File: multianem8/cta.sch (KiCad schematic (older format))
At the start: 281 parts, among them Q1 TIP41, Q10 TIP41, Q11 TIP41, Q12 TIP41, Q13 TIP41, Q14 TIP41, Q15 TIP41, Q16 TIP41, Q2 TIP41, Q3 TIP41, Q4 TIP41, Q5 TIP41, Q6 TIP41, Q7 TIP41, Q8 TIP41, Q9 TIP41, U1 LM324, U10 LM324, U11 LM324, U12 LM324, U13 LM324, U14 LM324, U15 LM324, U16 LM324, U2 LM324, U3 LM324, U4 LM324, U5 LM324, U6 LM324, U7 LM324, U8 LM324, U9 LM324

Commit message: Created the multiname8 board
I recycled the multinam16 board and the numbering of each anemometer's component is 1-4 and 9-12. I might (might...) change the numbering 9-12 to 5-8. The output is also inverted inthe flat cable coming out of the board.
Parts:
- removed CI13, CI14, CI15, CI16, CI5, CI6, CI7, CI8: 100n, Capacitor_THT:C_Rect_L7.2mm_W3.5mm_P5.00mm_FKS2_FKP2_MKS2_MKP2, symbol Device:C
- removed Cf13, Cf14, Cf15, Cf16, Cf5, Cf6, Cf7, Cf8: 1u, Capacitor_THT:CP_Radial_D5.0mm_P2.50mm, symbol Device:CP
- removed Cua13, Cua14, Cua15, Cua16, Cua5, Cua6, Cua7, Cua8, Cub13, Cub14, Cub15, Cub16, Cub5, Cub6, Cub7, Cub8: 100n, Capacitor_THT:C_Disc_D5.0mm_W2.5mm_P2.50mm, symbol Device:C
- removed Don13, Don14, Don15, Don16, Don5, Don6, Don7, Don8: 1N4148, Diode_THT:D_DO-35_SOD27_P7.62mm_Horizontal, symbol Diode:1N4148
- removed JOUT1, JOUT2: Conn_01x08, Connector_PinHeader_2.54mm:PinHeader_1x08_P2.54mm_Vertical, symbol Connector_Generic:Conn_01x08
- removed Jw13, Jw14, Jw15, Jw16, Jw5, Jw6, Jw7, Jw8: Conn_01x02, Connector_PinHeader_2.54mm:PinHeader_1x02_P2.54mm_Vertical, symbol Connector_Generic:Conn_01x02
- removed Q13, Q14, Q15, Q16, Q5, Q6, Q7, Q8: TIP41, Package_TO_SOT_THT:TO-220-3_Vertical, symbol Transistor_BJT:TIP41
- removed Ra13, Ra14, Ra15, Ra16, Ra5, Ra6, Ra7, Ra8: 100, Resistor_THT:R_Axial_DIN0207_L6.3mm_D2.5mm_P10.16mm_Horizontal, symbol Device:R
- removed Rb13, Rb14, Rb15, Rb16, Rb5, Rb6, Rb7, Rb8: 10, Resistor_THT:R_Axial_DIN0414_L11.9mm_D4.5mm_P15.24mm_Horizontal, symbol Device:R
- removed Rc13, Rc14, Rc15, Rc16, Rc5, Rc6, Rc7, Rc8: 1k, Resistor_THT:R_Axial_DIN0207_L6.3mm_D2.5mm_P10.16mm_Horizontal, symbol Device:R
- removed Rda13, Rda14, Rda15, Rda16, Rda5, Rda6, Rda7, Rda8: 100k, Resistor_THT:R_Axial_DIN0207_L6.3mm_D2.5mm_P10.16mm_Horizontal, symbol Device:R
- removed Rdb13, Rdb14, Rdb15, Rdb16, Rdb5, Rdb6, Rdb7, Rdb8: 20k, Resistor_THT:R_Axial_DIN0207_L6.3mm_D2.5mm_P10.16mm_Horizontal, symbol Device:R
- removed Rf13, Rf14, Rf15, Rf16, Rf5, Rf6, Rf7, Rf8, Rua13, Rua14, Rua15, Rua16, Rua5, Rua6, Rua7, Rua8, Rub13, Rub14, Rub15, Rub16, Rub5, Rub6, Rub7, Rub8: 10k, Resistor_THT:R_Axial_DIN0207_L6.3mm_D2.5mm_P10.16mm_Horizontal, symbol Device:R
- removed Rt13, Rt14, Rt15, Rt16, Rt5, Rt6, Rt7, Rt8: 2k, Resistor_THT:R_Axial_DIN0207_L6.3mm_D2.5mm_P10.16mm_Horizontal, symbol Device:R
- removed U13, U14, U15, U16, U5, U6, U7, U8: LM324, Package_DIP:DIP-14_W7.62mm_LongPads, symbol Amplifier_Operational:LM324
- added JOUT1: Conn_01x09, Connector_PinHeader_2.54mm:PinHeader_1x09_P2.54mm_Vertical, symbol Connector_Generic:Conn_01x09
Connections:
- net GND: now also JOUT1.9 (Pin_9)
- net VO1: now also JOUT1.1 (Pin_1)
- net VO10: now also JOUT1.7 (Pin_7)
- net VO11: now also JOUT1.6 (Pin_6)
- net VO12: now also JOUT1.5 (Pin_5)
- net VO2: now also JOUT1.2 (Pin_2)
- net VO3: now also JOUT1.3 (Pin_3)
- net VO4: now also JOUT1.4 (Pin_4)
- net VO9: now also JOUT1.8 (Pin_8)

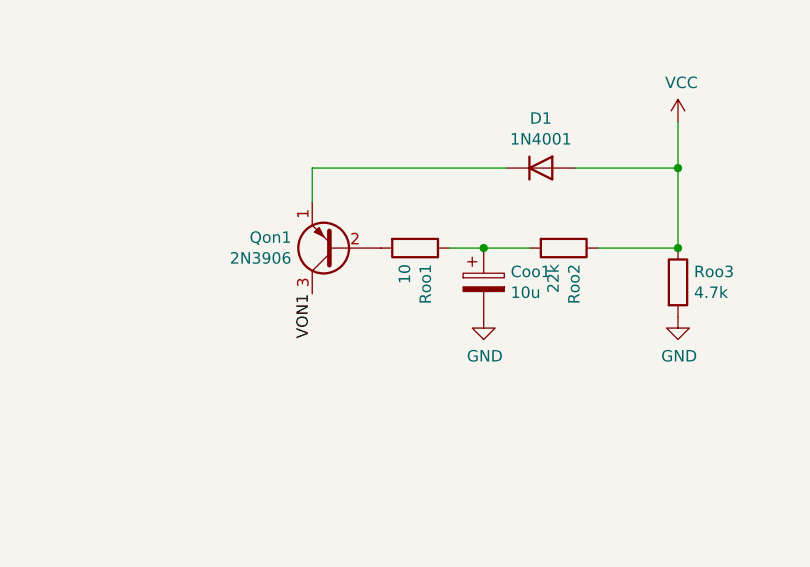
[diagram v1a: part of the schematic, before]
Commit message: Created gerber files for fabrication
I will try to build the board on some fab.
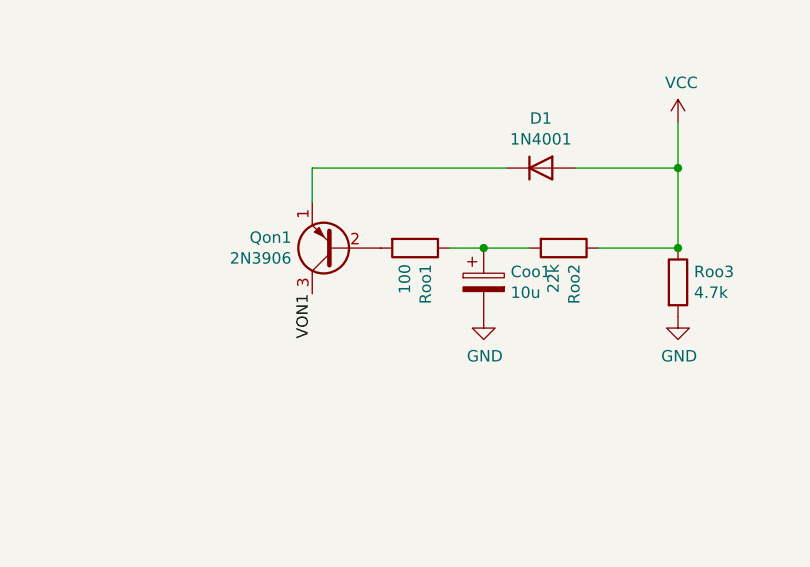
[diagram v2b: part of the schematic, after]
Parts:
- Roo1: value 10 -> 100
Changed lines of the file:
@@
 P 8450 4700
 F 0 "Roo1" H 8520 4746 50  0000 L CNN
-F 1 "10" H 8520 4655 50  0000 L CNN
+F 1 "100" H 8520 4655 50  0000 L CNN
 F 2 "Resistor_THT:R_Axial_DIN0207_L6.3mm_D2.5mm_P10.16mm_Horizontal" V 8380 4700 50  0001 C CNN
 F 3 "~" H 8450 4700 50  0001 C CNN
